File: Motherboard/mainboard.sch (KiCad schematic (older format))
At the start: 51 parts, among them IC1 BMX160, J1 Conn_01x01, J2 10118194-0001LF, J28 Conn_01x01, J29 Conn_01x01, J3 Micro_SD_Card, J30 Conn_01x01, J4 xf2m-2415-1a, J5 XF2M-1015-1A, J6 U.FL-R-SMT-1, J7 U.FL-R-SMT-1, J8 Conn_01x01, SW1 KMR231NG LFS, U1 RFM95W-915S2, U2 ATSAMD51G_TQFN48, U3 DRV8848, U4 TPS82740BSIPR, U5 DRV8848, U6 MAX708RESA-T, U8 RFM95W-915S2

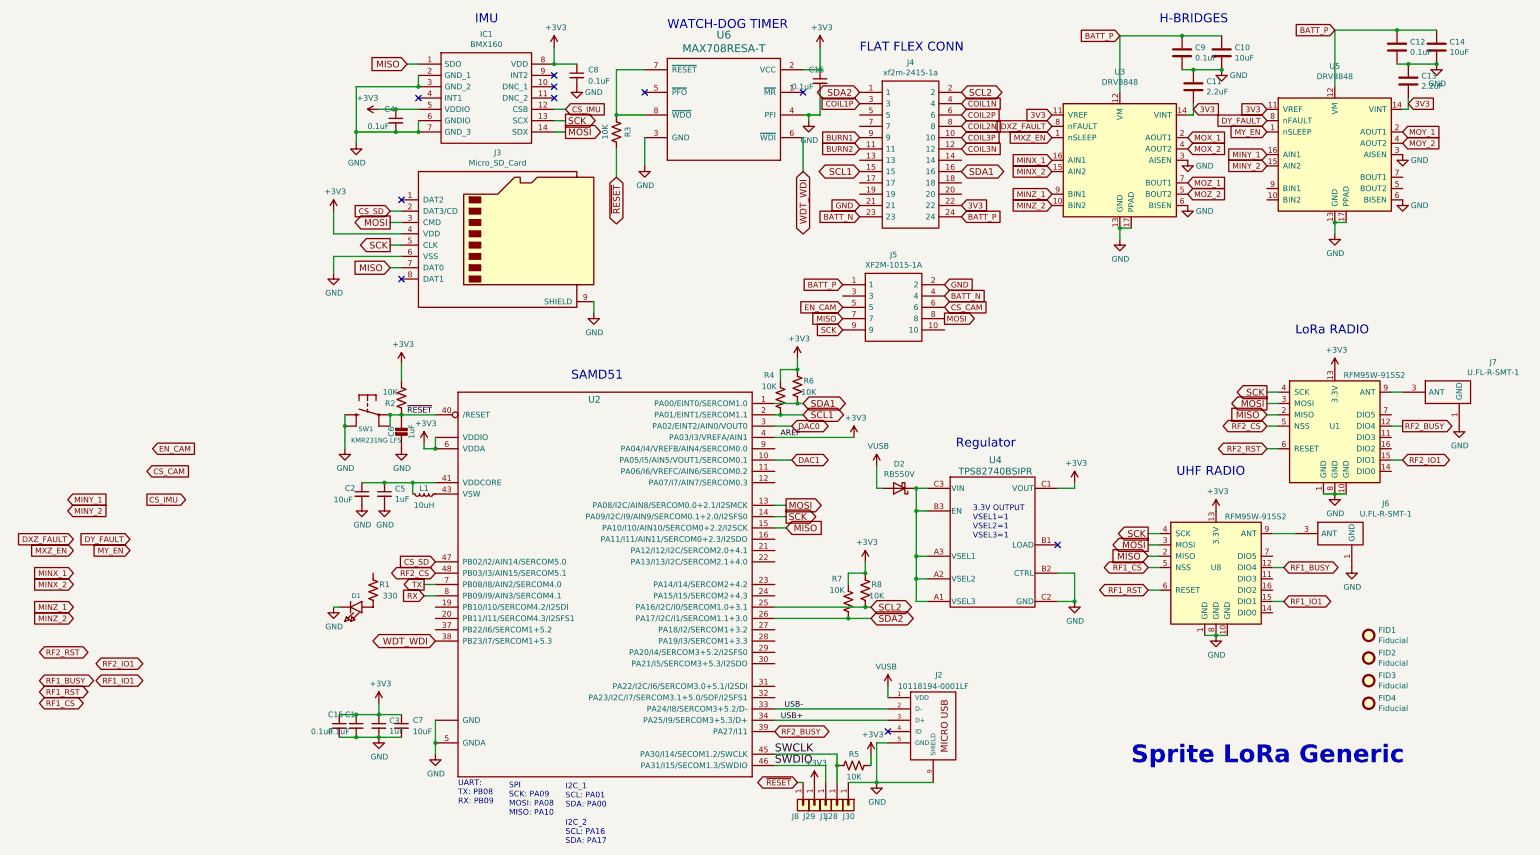
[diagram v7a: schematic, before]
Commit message: routed except for connectors
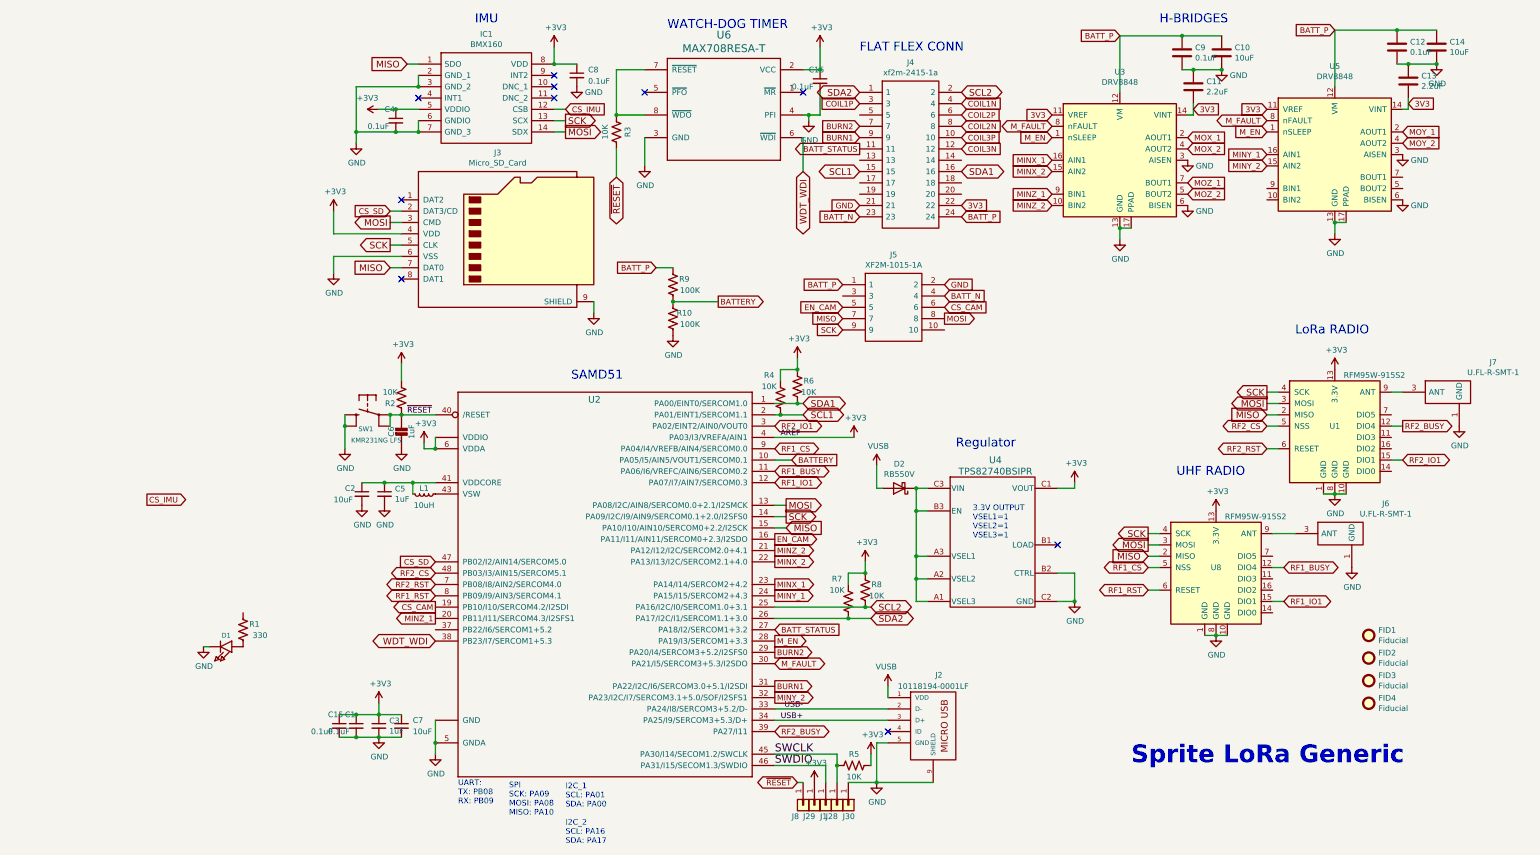
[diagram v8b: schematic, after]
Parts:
- added R10, R9: 100K, Resistor_SMD:R_0402_1005Metric, symbol mainboard-rescue:R_US-Device
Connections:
- net DAC0 is gone; now on net RF2_IO1: U2.3 (PA02/EINT2/AIN0/VOUT0)
- net DXZ_FAULT is gone; now on net M_FAULT: U3.8 (nFAULT)
- net DY_FAULT is gone; now on net M_FAULT: U5.8 (nFAULT)
- net MXZ_EN is gone; now on net M_EN: U3.1 (nSLEEP)
- net MY_EN is gone; now on net M_EN: U5.1 (nSLEEP)
- net RX is gone; now on net RF1_RST: U2.8 (PB09/I9/AIN3/SERCOM4.1)
- net TX is gone; now on net RF2_RST: U2.7 (PB08/I8/AIN2/SERCOM4.0)
- net BATT_P: now also R9.2
- net BURN1: now also U2.31 (PA22/I2C/I6/SERCOM3.0+5.1/I2SDI)
- net BURN2: now also J4.7, U2.29 (PA20/I4/SERCOM3+5.2/I2SFS0); no longer J4.11
- net CS_CAM: now also U2.19 (PB10/I10/SERCOM4.2/I2SDI)
- net EN_CAM: now also U2.16 (PA11/I11/AIN11/SERCOM0+2.3/I2SDO)
- net GND: now also R10.1
- net MINX_1: now also U2.23 (PA14/I14/SERCOM2+4.2)
- net MINX_2: now also U2.22 (PA13/I13/I2C/SERCOM2.1+4.0)
- net MINY_1: now also U2.24 (PA15/I15/SERCOM2+4.3)
- net MINY_2: now also U2.32 (PA23/I2C/I7/SERCOM3.1+5.0/SOF/I2SFS1)
- net MINZ_1: now also U2.20 (PB11/I11/SERCOM4.3/I2SFS1)
- net MINZ_2: now also U2.21 (PA12/I12/I2C/SERCOM2.0+4.1)
- net RF1_BUSY: now also U2.11 (PA06/I6/VREFC/AIN6/SERCOM0.2)
- net RF1_CS: now also U2.9 (PA04/I4/VREFB/AIN4/SERCOM0.0)
- net RF1_IO1: now also U2.12 (PA07/I7/AIN7/SERCOM0.3)
- net BATT_STATUS: now reaches U2.27 (PA18/I2/SERCOM1+3.2)
- net BATT_STATUS: now also J4.11
- net M_EN: now reaches U2.28 (PA19/I3/SERCOM1+3.3)
- net M_FAULT: now reaches U2.30 (PA21/I5/SERCOM3+5.3/I2SDO)
- net DAC1 renamed BATTERY
- net BATTERY: now also R10.2, R9.1
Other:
- moved on the sheet: D1, R1
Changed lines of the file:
@@
 L mainboard-rescue:R_US-Device R1
 U 1 1 5C3B885A
-P 900 5650
-F 0 "R1" H 800 5600 50  0000 C CNN
-F 1 "330" H 750 5700 50  0000 C CNN
-F 2 "Resistor_SMD:R_0402_1005Metric" V 940 5640 50  0001 C CNN
-F 3 "~" H 900 5650 50  0001 C CNN
-	1    900  5650
+P -250 6000
+F 0 "R1" H -350 5950 50  0000 C CNN
+F 1 "330" H -400 6050 50  0000 C CNN
+F 2 "Resistor_SMD:R_0402_1005Metric" V -210 5990 50  0001 C CNN
+F 3 "~" H -250 6000 50  0001 C CNN
+	1    -250 6000
 	-1   0    0    1
 $EndComp
@@
 L mainboard-rescue:LED0805_NOOUTLINE- D?
 U 1 1 5C3B8860
-P 700 5800
+P -450 6150
 AR Path="/5BCFDB7D/5C3B8860" Ref="D?"  Part="1"
 AR Path="/5C3B8860" Ref="D1"  Part="1"
-F 0 "D1" H 650 5700 42  0000 C CNN
-F 1 "GREEN" H 550 6000 42  0001 C CNN
-F 2 "LED_SMD:LED_0603_1608Metric" H 700 5800 50  0001 C CNN
-F 3 "" H 700 5800 50  0001 C CNN
-	1    700  5800
+F 0 "D1" H -500 6050 42  0000 C CNN
+F 1 "GREEN" H -600 6350 42  0001 C CNN
+F 2 "LED_SMD:LED_0603_1608Metric" H -450 6150 50  0001 C CNN
+F 3 "" H -450 6150 50  0001 C CNN
+	1    -450 6150
 	-1   0    0    1
 $EndComp
@@
 Wire Wire Line
 	6950 5500 7100 5500
-Wire Wire Line
-	1450 5600 1350 5600
-Wire Wire Line
-	1450 5700 1350 5700
-Text GLabel 1350 5700 0    50   Input ~ 0
-RX
-Text GLabel 1350 5600 0    50   Output ~ 0
-TX
 Connection ~ 5000 7200
 Wire Wire Line
@@
 Wire Wire Line
 	5700 4950 5700 5350
-Text GLabel 4600 4200 2    50   BiDi ~ 0
-DAC0
 $Comp
 L power:+3V3 #PWR0103
@@
 L power:GND #PWR0121
 U 1 1 5DB132FE
-P 550 5800
-F 0 "#PWR0121" H 550 5550 50  0001 C CNN
-F 1 "GND" H 555 5627 50  0000 C CNN
-F 2 "" H 550 5800 50  0001 C CNN
-F 3 "" H 550 5800 50  0001 C CNN
-	1    550  5800
-	1    0    0    -1
-$EndComp
-Wire Wire Line
-	550  5800 600  5800
+P -600 6150
+F 0 "#PWR0121" H -600 5900 50  0001 C CNN
+F 1 "GND" H -595 5977 50  0000 C CNN
+F 2 "" H -600 6150 50  0001 C CNN
+F 3 "" H -600 6150 50  0001 C CNN
+	1    -600 6150
+	1    0    0    -1
+$EndComp
+Wire Wire Line
+	-600 6150 -550 6150
 $Comp
 L power:GND #PWR0122
@@
 Wire Wire Line
 	8950 5450 8850 5450
-Text GLabel 4600 4500 2    50   BiDi ~ 0
-DAC1
+Text GLabel 4600 4500 2    50   Input ~ 0
+BATTERY
 $Comp
 L mainboard-rescue:Conn_01x01-Connector_Generic J28
@@
 Wire Wire Line
 	7500 750  8050 750
-Text GLabel 6900 1550 0    50   Input ~ 0
-DXZ_FAULT
-Text GLabel 6900 1650 0    50   Input ~ 0
-MXZ_EN
+Text GLabel 6900 1550 0    50   BiDi ~ 0
+M_FAULT
 Text GLabel 6900 1850 0    50   Input ~ 0
 MINX_1
@@
 Wire Wire Line
 	9400 700  9950 700
-Text GLabel 8800 1500 0    50   Input ~ 0
-DY_FAULT
 Text GLabel 8800 1600 0    50   Input ~ 0
-MY_EN
+M_EN
 Text GLabel 8800 1800 0    50   Input ~ 0
 MINY_1
@@
 Text GLabel 5950 3050 2    50   Input ~ 0
 BATT_N
-Text GLabel -1100 4600 2    50   Input ~ 0
+Text GLabel 1450 5800 0    50   Output ~ 0
 CS_CAM
 Connection ~ 1450 7000
@@
 Wire Wire Line
 	1450 7100 1450 7000
-Connection ~ 1450 4400
 Wire Wire Line
 	4900 7200 4450 7200
@@
 	4450 4300 5150 4300
 Wire Wire Line
-	4450 4200 4600 4200
-Wire Wire Line
 	5300 5900 5100 5900
-$Comp
-L mainboard-rescue:ATSAMD51G_TQFN48- U2
-U 1 1 5C58A0F8
-P 2950 5900
-F 0 "U2" H 2800 7800 59  0000 L BNN
-F 1 "ATSAMD51G_TQFN48" H 1850 8000 59  0001 L BNN
-F 2 "ATSAMD51G19A-MU:QFN50P700X700X90-49N-D" H 2950 5900 50  0001 C CNN
-F 3 "" H 2950 5900 50  0001 C CNN
-	1    2950 5900
-	1    0    0    -1
-$EndComp
-Text GLabel -1050 4400 2    50   Input ~ 0
+Text GLabel 4450 5200 2    50   Output ~ 0
 EN_CAM
 Text GLabel 5300 5800 2    59   BiDi ~ 0
@@
 Text GLabel 5200 1650 0    50   Input ~ 0
 BURN1
-Text GLabel 5200 1750 0    50   Input ~ 0
+Text GLabel 5200 1550 0    50   Input ~ 0
 BURN2
 Text GLabel 5200 1350 0    50   Input ~ 0
@@
 Wire Wire Line
 	4650 7350 4700 7350
-Text GLabel -1750 5200 0    50   Input ~ 0
-DXZ_FAULT
-Text GLabel -1750 5300 0    50   Input ~ 0
-MXZ_EN
-Text GLabel -1750 5500 0    50   Input ~ 0
+Text GLabel 4450 5600 2    50   Output ~ 0
 MINX_1
-Text GLabel -1750 5600 0    50   Input ~ 0
-MINX_2
-Text GLabel -1750 5800 0    50   Input ~ 0
+Text GLabel 4450 5300 2    50   Output ~ 0
+MINZ_2
+Text GLabel 1450 5900 0    50   Output ~ 0
 MINZ_1
-Text GLabel -1750 5900 0    50   Input ~ 0
-MINZ_2
-Text GLabel -1250 5200 0    50   Input ~ 0
-DY_FAULT
-Text GLabel -1250 5300 0    50   Input ~ 0
-MY_EN
-Text GLabel -1800 4850 2    50   Input ~ 0
+Text GLabel 4450 5700 2    50   Output ~ 0
 MINY_1
-Text GLabel -1800 4950 2    50   Input ~ 0
-MINY_2
 $Comp
 L Mechanical:Fiducial FID1
@@
 	1    0    0    -1
 $EndComp
-Text GLabel -2050 6450 2    50   BiDi ~ 0
+Text GLabel 4450 4600 2    50   BiDi ~ 0
 RF1_BUSY
-Text GLabel -2050 6550 2    50   BiDi ~ 0
+Text GLabel 1450 5700 0    50   BiDi ~ 0
 RF1_RST
-Text GLabel -2050 6650 2    50   BiDi ~ 0
+Text GLabel 4450 4400 2    50   BiDi ~ 0
 RF1_CS
-Text GLabel -1550 6450 2    50   BiDi ~ 0
-RF1_IO1
 Text GLabel 8800 4200 0    50   BiDi ~ 0
 RF2_CS
@@
 Text GLabel 1450 5500 0    50   BiDi ~ 0
 RF2_CS
-Text GLabel -1550 6300 2    50   BiDi ~ 0
+Text GLabel 4450 4200 2    50   BiDi ~ 0
 RF2_IO1
-Text GLabel -2050 6200 2    50   BiDi ~ 0
+Text GLabel 1450 5600 0    50   BiDi ~ 0
 RF2_RST
 Text GLabel 4450 6900 2    50   BiDi ~ 0
@@
 Text GLabel 1450 5400 0    50   Input ~ 0
 CS_SD
+$Comp
+L mainboard-rescue:R_US-Device R10
+U 1 1 5DC613D0
+P 3550 3250
+F 0 "R10" H 3450 3200 50  0000 C CNN
+F 1 "100K" H 3400 3300 50  0000 C CNN
+F 2 "Resistor_SMD:R_0402_1005Metric" V 3590 3240 50  0001 C CNN
+F 3 "~" H 3550 3250 50  0001 C CNN
+	1    3550 3250
+	-1   0    0    1
+$EndComp
+$Comp
+L mainboard-rescue:R_US-Device R9
+U 1 1 5DC61A47
+P 3550 2950
+F 0 "R9" H 3450 2900 50  0000 C CNN
+F 1 "100K" H 3400 3000 50  0000 C CNN
+F 2 "Resistor_SMD:R_0402_1005Metric" V 3590 2940 50  0001 C CNN
+F 3 "~" H 3550 2950 50  0001 C CNN
+	1    3550 2950
+	-1   0    0    1
+$EndComp
+Text GLabel 3400 2800 0    50   Input ~ 0
+BATT_P
+Wire Wire Line
+	3400 2800 3550 2800
+Wire Wire Line
+	3550 3100 3950 3100
+Connection ~ 3550 3100
+$Comp
+L power:GND #PWR01
+U 1 1 5DC7783A
+P 3550 3400
+F 0 "#PWR01" H 3550 3150 50  0001 C CNN
+F 1 "GND" H 3555 3227 50  0000 C CNN
+F 2 "" H 3550 3400 50  0001 C CNN
+F 3 "" H 3550 3400 50  0001 C CNN
+	1    3550 3400
+	1    0    0    -1
+$EndComp
+Text GLabel 3950 3100 2    50   Output ~ 0
+BATTERY
+Text GLabel 4450 6000 2    50   Input ~ 0
+BATT_STATUS
+Text GLabel 5200 1750 0    50   Output ~ 0
+BATT_STATUS
+Text GLabel 4450 4700 2    50   BiDi ~ 0
+RF1_IO1
+Text GLabel 8800 1500 0    50   BiDi ~ 0
+M_FAULT
+Text GLabel 4450 6300 2    50   BiDi ~ 0
+M_FAULT
+Text GLabel 6900 1650 0    50   Input ~ 0
+M_EN
+Text GLabel 4450 6500 2    50   Output ~ 0
+BURN1
+Text GLabel 4450 6200 2    50   Output ~ 0
+BURN2
+Text GLabel 4450 6100 2    50   Output ~ 0
+M_EN
+Text GLabel 4450 6600 2    50   Output ~ 0
+MINY_2
+Text GLabel 4450 5400 2    50   Output ~ 0
+MINX_2
+Connection ~ 1450 4400
+$Comp
+L mainboard-rescue:ATSAMD51G_TQFN48- U2
+U 1 1 5C58A0F8
+P 2950 5900
+F 0 "U2" H 2800 7800 59  0000 L BNN
+F 1 "ATSAMD51G_TQFN48" H 1850 8000 59  0001 L BNN
+F 2 "ATSAMD51G19A-MU:QFN50P700X700X90-49N-D" H 2950 5900 50  0001 C CNN
+F 3 "" H 2950 5900 50  0001 C CNN
+	1    2950 5900
+	1    0    0    -1
+$EndComp
 $EndSCHEMATC
